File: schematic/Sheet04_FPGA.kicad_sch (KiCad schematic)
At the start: 12 parts

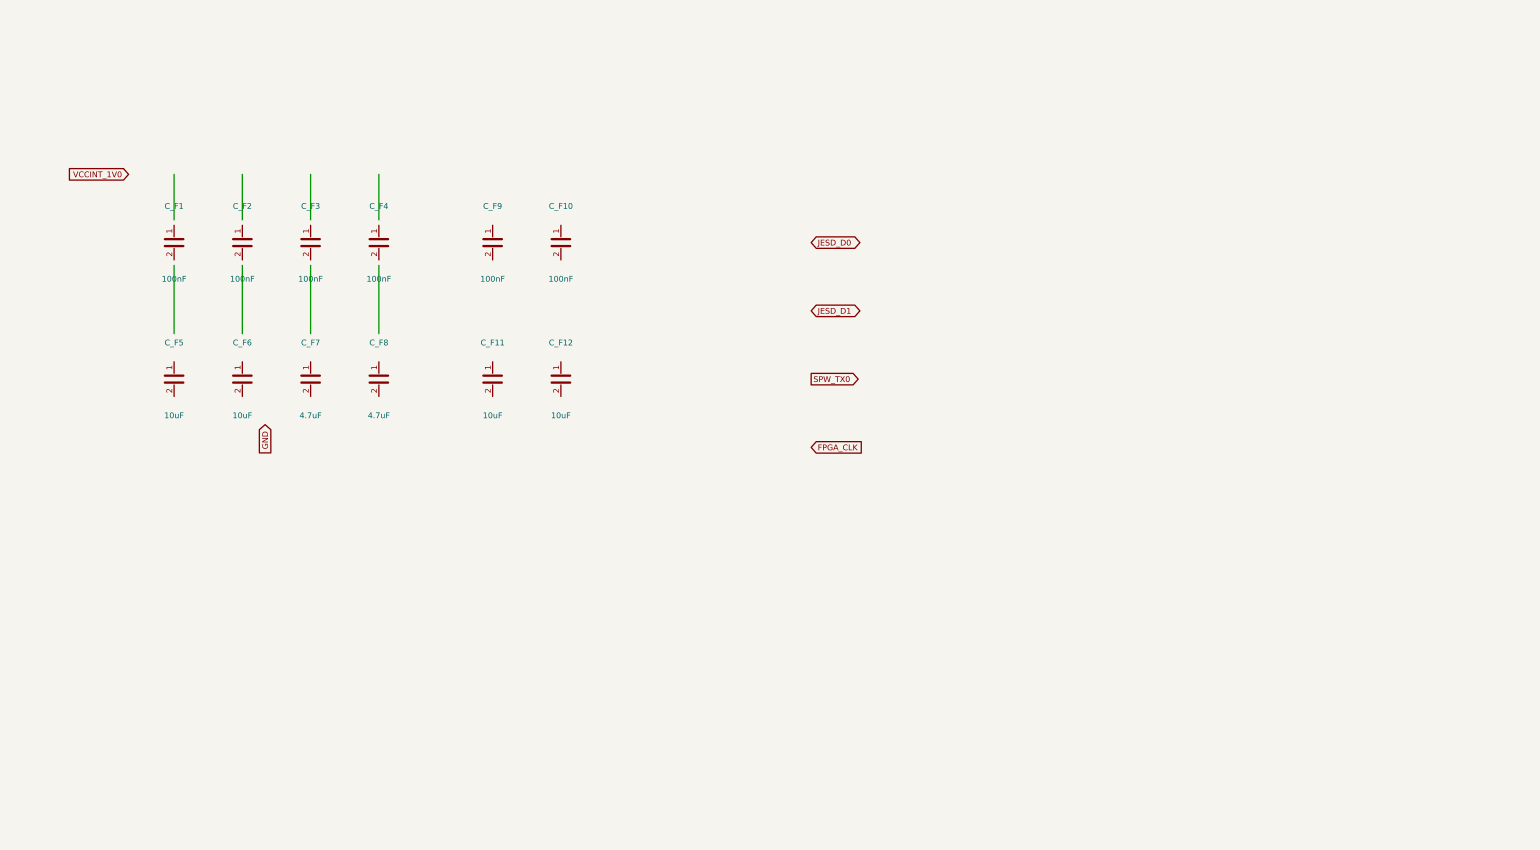
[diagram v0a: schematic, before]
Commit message: feat: real IC schematics with proper pin connections
- ADC12DJ5200-SP: 20 left pins (power, SPI, analog) + 21 right pins (JESD204C)
- XQRVC1902-SP: 19 left pins (power) + 30 right pins (JTAG, SPW, JESD, config)
- TPS7H5002-SP: 9 left + 7 right pins (buck converter 1.0V core)
- ISL70003ASEH: 7 left + 5 right (buck 1.8V/3.3V)
- LMX2615-SP: 8+8 pins (PLL synthesizer)
- LMK04832-SP: 12+12 pins (clock distributor)
- TPS7H1111-SP / TPS7H1121-SP: 3+3 pins (LDOs)
- TPS7H3014-SP: 4+4 pins (sequencer)
- INA214-SP: 3+2 pins (current sense)
- CVHD-950: 3+2 pins (VCXO)

Sheets:
- 02: SMA→50Ω match→anti-alias→ADC analog input
- 03: ADC decoupling, JESD outputs, SPI control
- 04: FPGA 14x decoupling caps, JTAG, SPW, JESD
- 05: Crystek→LMX2615→LMK04832→ADC+FPGA clock tree
- 06-09: Power input, TPS7H5002 buck 1.0V, ISL70003A buck 1.8V/3.3V
- 10-12: LDO 1.0V analog, 1.8V digital, 2.5V clock
- 13: 2x TPS7H3014 power sequencer
- 14: JTAG/SPW/UART connectors
- 15-17: Test points, decoupling, power tree diagram

All 17 sheets export via kicad-cli, merged PDF: 1.1MB
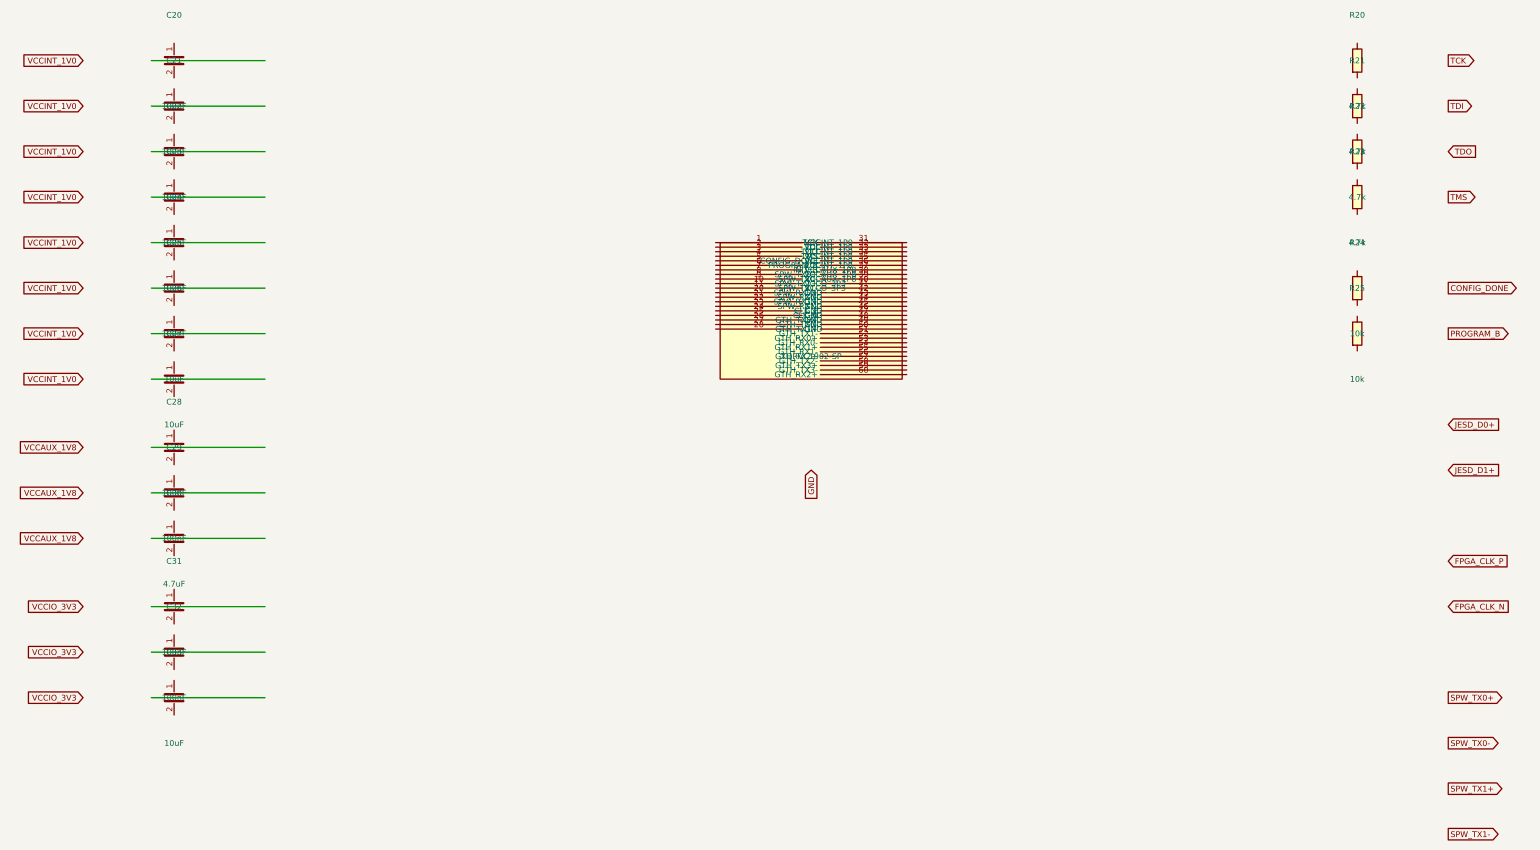
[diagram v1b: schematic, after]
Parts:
- removed C_F1, C_F10, C_F2, C_F3, C_F4, C_F9: 100nF, Capacitor_SMD:C_0402_1005Metric, symbol Device:C
- removed C_F11, C_F12, C_F5, C_F6: 10uF, Capacitor_SMD:C_0603_1608Metric, symbol Device:C
- removed C_F7, C_F8: 4.7uF, Capacitor_SMD:C_0402_1005Metric, symbol Device:C
- added C20, C21, C22, C23, C24, C25, C28, C29, C31, C32: 100nF, C_0402, symbol Device:C
- added C26, C27, C33: 10uF, C_0603, symbol Device:C
- added C30: 4.7uF, C_0402, symbol Device:C
- added R20, R21, R22, R23: 4.7k, R_0402, symbol Device:R
- added R24, R25: 10k, R_0402, symbol Device:R
- added U2: XQRVC1902-SP, BGA-1156, symbol Custom:XQRVC1902-SP

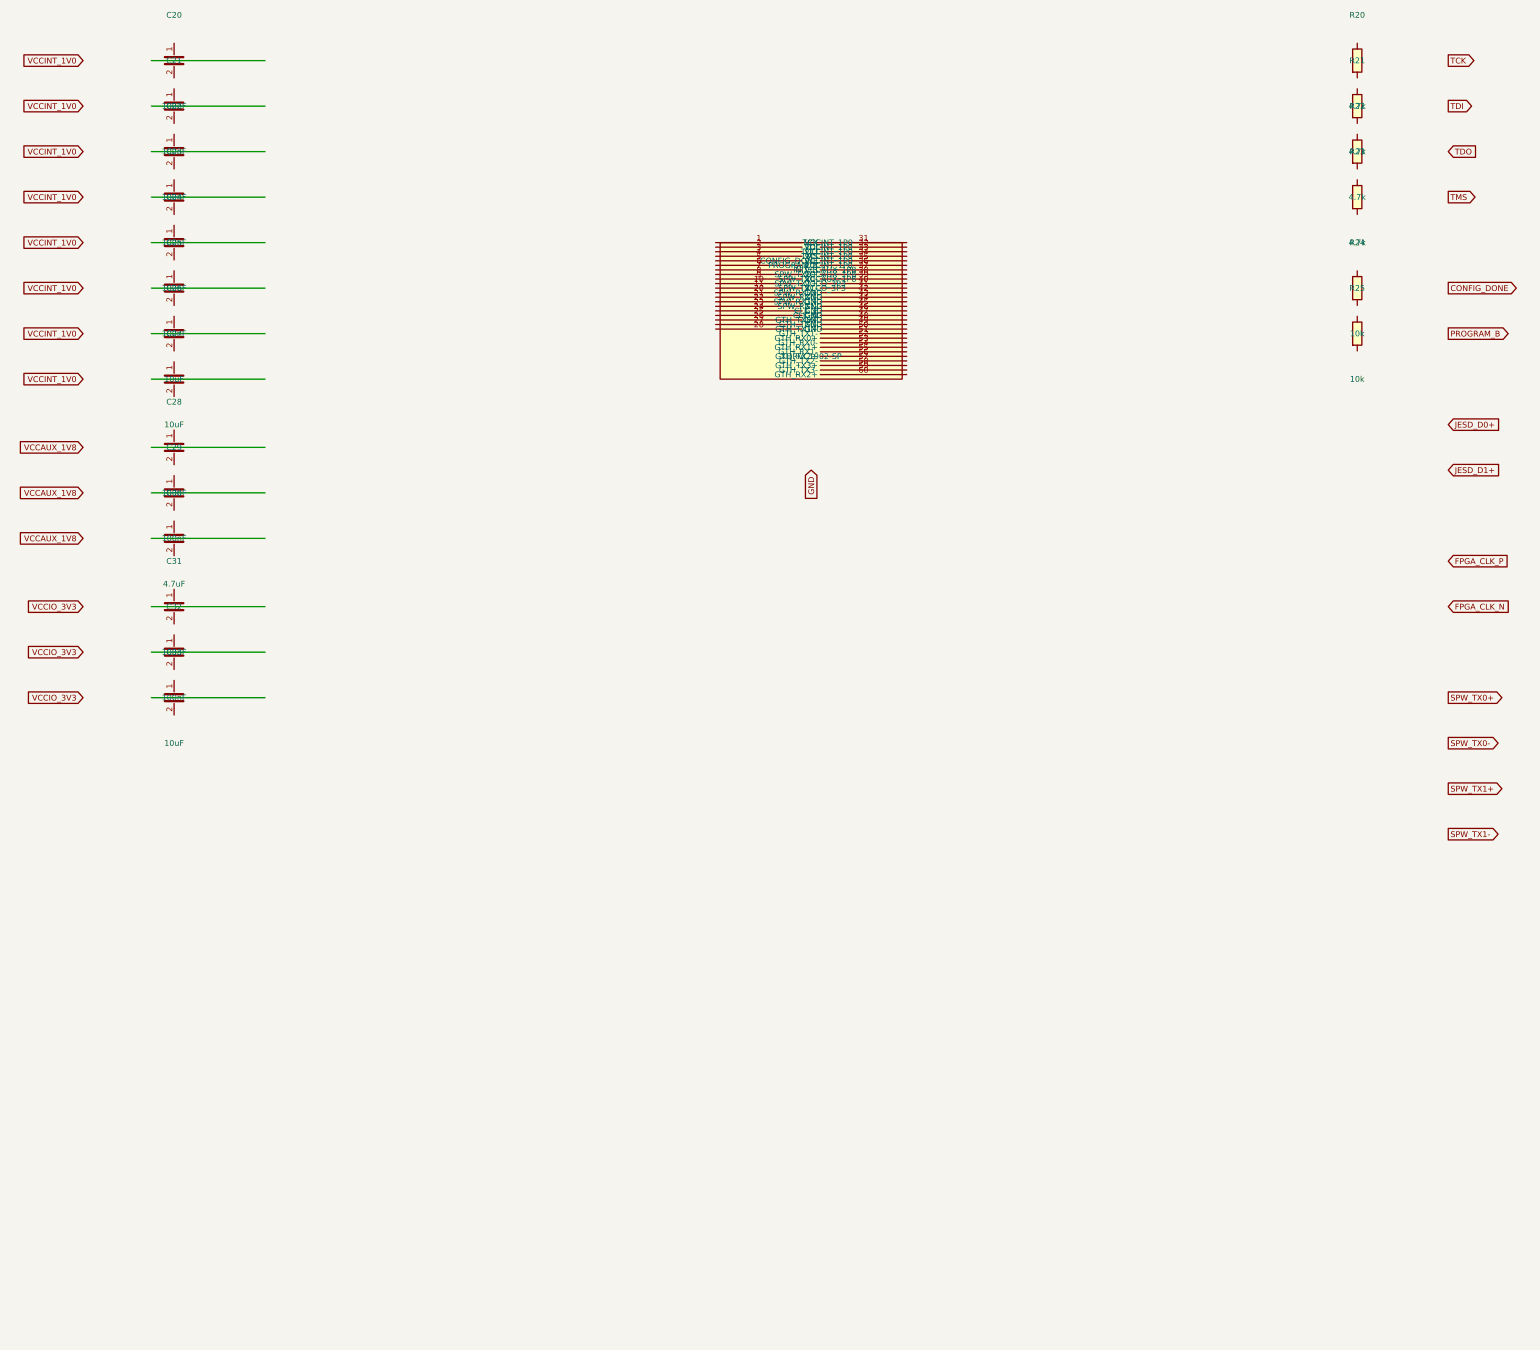
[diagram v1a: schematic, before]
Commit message: feat: schematic sheets with datasheet-correct IC pinouts and connections
- Downloaded 10 official datasheets (TI, Renesas, Crystek) for all major ICs
- Extracted exact pin configurations from PDF pin tables
- Generated Custom_ICs.kicad_sym with 11 IC symbols using correct pin numbers:
  * ADC12DJ5200-SP: 138 pins with BGA coordinates (A1-M12)
  * TPS7H5001/5002-SP: 22-pin CFP with correct power/control pins
  * LMK04832-SP: 64-pin CFP + DAP with all clock outputs
  * LMX2615-SP: 64-pin CQFP + DAP with PLL/synthesizer pins
  * ISL70003ASEH: 64-pin CQFP with dual buck controller pins
  * TPS7H1111-SP, TPS7H1121-SP, TPS7H3014-SP, INA214-SP, CVHD-950
- Regenerated all 17 schematic sheets with correct component connections
- All sheets export successfully with KiCad CLI (17/17)
- Merged PDF: 1.3MB, 17 pages
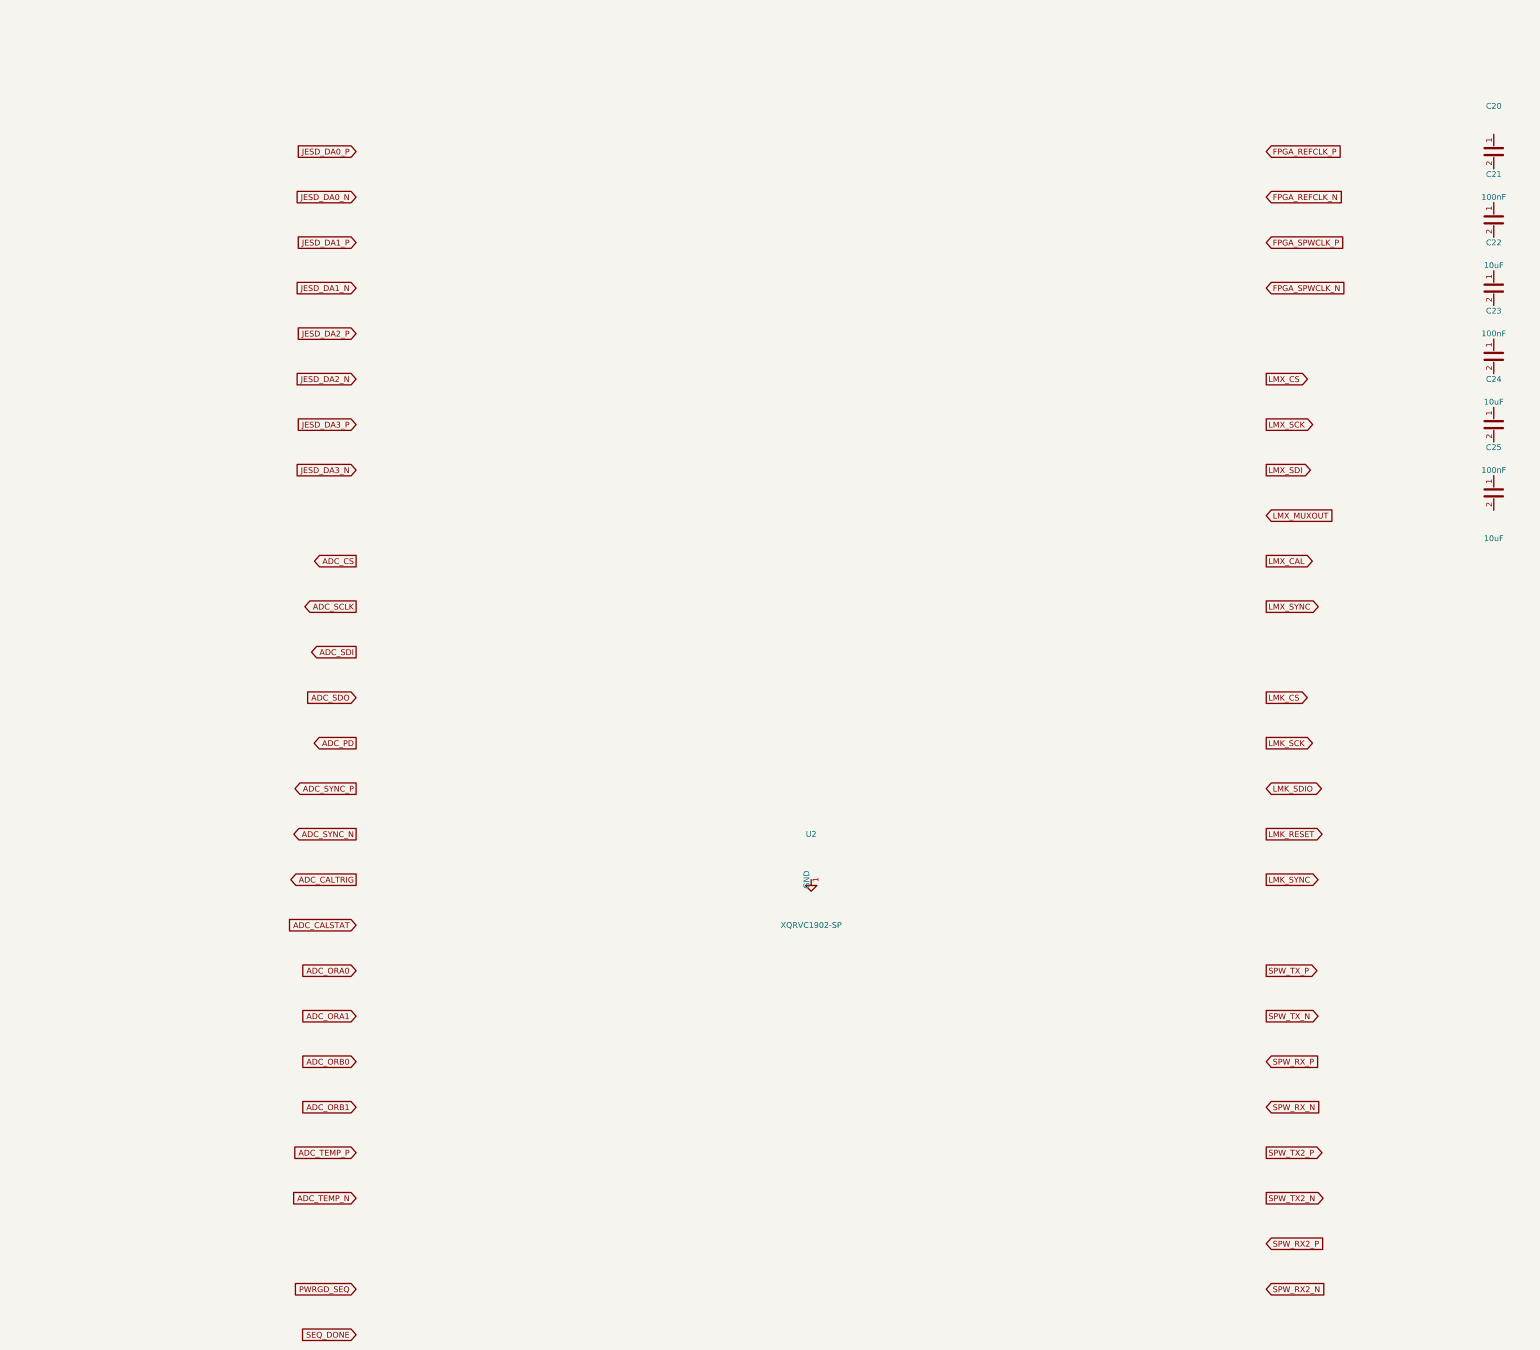
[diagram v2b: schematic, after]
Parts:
- removed C26, C27, C33: 10uF, C_0603, symbol Device:C
- removed C28, C29, C31, C32: 100nF, C_0402, symbol Device:C
- removed C30: 4.7uF, C_0402, symbol Device:C
- removed R20, R21, R22, R23: 4.7k, R_0402, symbol Device:R
- removed R24, R25: 10k, R_0402, symbol Device:R
- removed U2: XQRVC1902-SP, BGA-1156, symbol Custom:XQRVC1902-SP
- C21, C23, C25: value 100nF -> 10uF; footprint C_0402 -> C_0603
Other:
- title: X-Band Digital Module 20x20cm -> X-Band FPGA XQRVC1902-SP

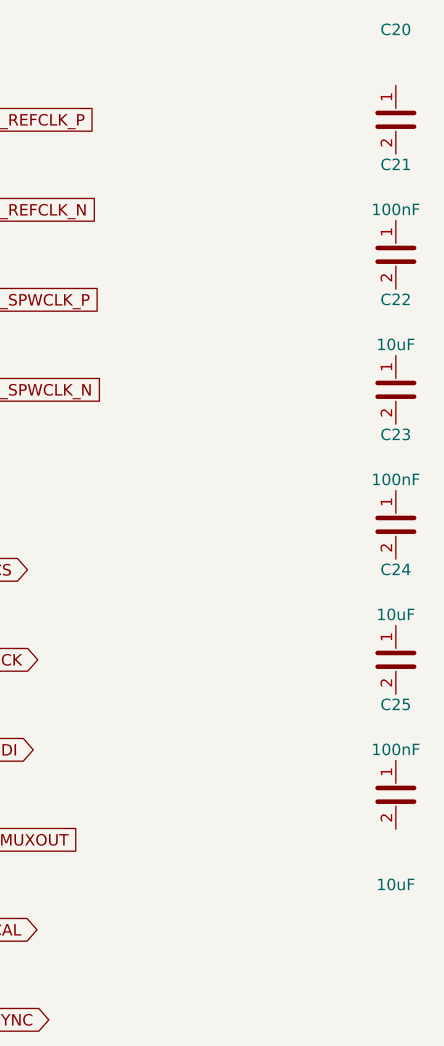
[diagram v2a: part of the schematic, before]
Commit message: feat: add 745 wire connections linking all IC pins to labels and power symbols
- Added stub wires from every component pin to net labels/global_labels
- Power pins connected to correct power symbols (GND, +1V0, +1V8, +3V3, etc.)
- Signal pins connected to labeled nets matching design spec
- Global labels for cross-sheet signals (JESD, SPI, clock, SpaceWire)
- Fixed missing +3V3 power symbol definitions in 5 sheets
- All 17 sheets export successfully with KiCad CLI (17/17 OK)
- Merged PDF: 3.1MB, 17 pages with visible wire connections
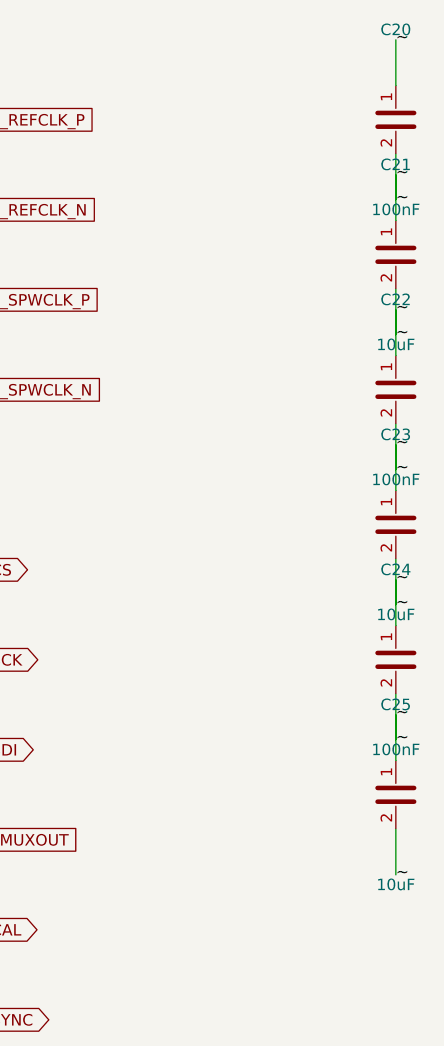
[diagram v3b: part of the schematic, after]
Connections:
- net ~: now reaches C24.1
- net ~: now also C20.1, C20.2, C21.1, C21.2, C22.1, C22.2, C23.1, C23.2, C24.2, C25.1, C25.2
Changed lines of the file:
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@@
     (pin "1")
     (pin "2")
-  )  (sheet_instances (path "/" (page "1")))
+  )
+  (wire (pts (xy 350.00 43.81) (xy 350.00 48.89)) (stroke (width 0) (type default)))
+  (label "~" (at 350.00 48.89 0) (effects (font (size 1.27 1.27))))
+  (wire (pts (xy 350.00 36.19) (xy 350.00 31.11)) (stroke (width 0) (type default)))
+  (label "~" (at 350.00 31.11 0) (effects (font (size 1.27 1.27))))
+  (wire (pts (xy 350.00 58.81) (xy 350.00 63.89)) (stroke (width 0) (type default)))
+  (label "~" (at 350.00 63.89 0) (effects (font (size 1.27 1.27))))
+  (wire (pts (xy 350.00 51.19) (xy 350.00 46.11)) (stroke (width 0) (type default)))
+  (label "~" (at 350.00 46.11 0) (effects (font (size 1.27 1.27))))
+  (wire (pts (xy 350.00 73.81) (xy 350.00 78.89)) (stroke (width 0) (type default)))
+  (label "~" (at 350.00 78.89 0) (effects (font (size 1.27 1.27))))
+  (wire (pts (xy 350.00 66.19) (xy 350.00 61.11)) (stroke (width 0) (type default)))
+  (label "~" (at 350.00 61.11 0) (effects (font (size 1.27 1.27))))
+  (wire (pts (xy 350.00 88.81) (xy 350.00 93.89)) (stroke (width 0) (type default)))
+  (label "~" (at 350.00 93.89 0) (effects (font (size 1.27 1.27))))
+  (wire (pts (xy 350.00 81.19) (xy 350.00 76.11)) (stroke (width 0) (type default)))
+  (label "~" (at 350.00 76.11 0) (effects (font (size 1.27 1.27))))
+  (wire (pts (xy 350.00 103.81) (xy 350.00 108.89)) (stroke (width 0) (type default)))
+  (label "~" (at 350.00 108.89 0) (effects (font (size 1.27 1.27))))
+  (wire (pts (xy 350.00 96.19) (xy 350.00 91.11)) (stroke (width 0) (type default)))
+  (label "~" (at 350.00 91.11 0) (effects (font (size 1.27 1.27))))
+  (wire (pts (xy 350.00 118.81) (xy 350.00 123.89)) (stroke (width 0) (type default)))
+  (label "~" (at 350.00 123.89 0) (effects (font (size 1.27 1.27))))
+  (wire (pts (xy 350.00 111.19) (xy 350.00 106.11)) (stroke (width 0) (type default)))
+  (label "~" (at 350.00 106.11 0) (effects (font (size 1.27 1.27))))
+  (sheet_instances (path "/" (page "1")))
 )
